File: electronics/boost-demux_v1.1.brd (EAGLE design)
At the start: 82.5 x 57.1 mm, 46 parts, among them M1 6-32_MOUNT, M2 6-32_MOUNT, M3 6-32_MOUNT, M4 6-32_MOUNT, Q1 ON_FDD4141, U1 TI_TPS55330, U2 4067D, U5 AVAGO_ACPL-217

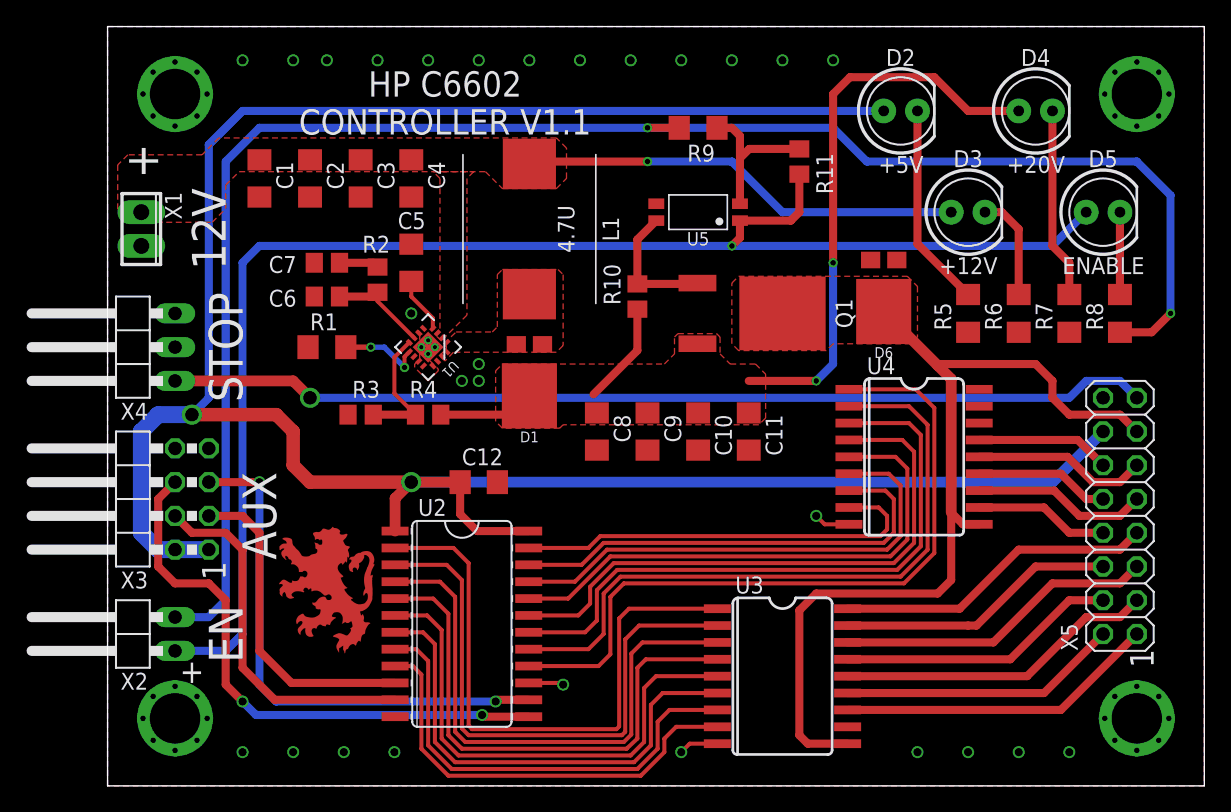
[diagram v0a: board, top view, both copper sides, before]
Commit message: Electronics v1.1 draft updates
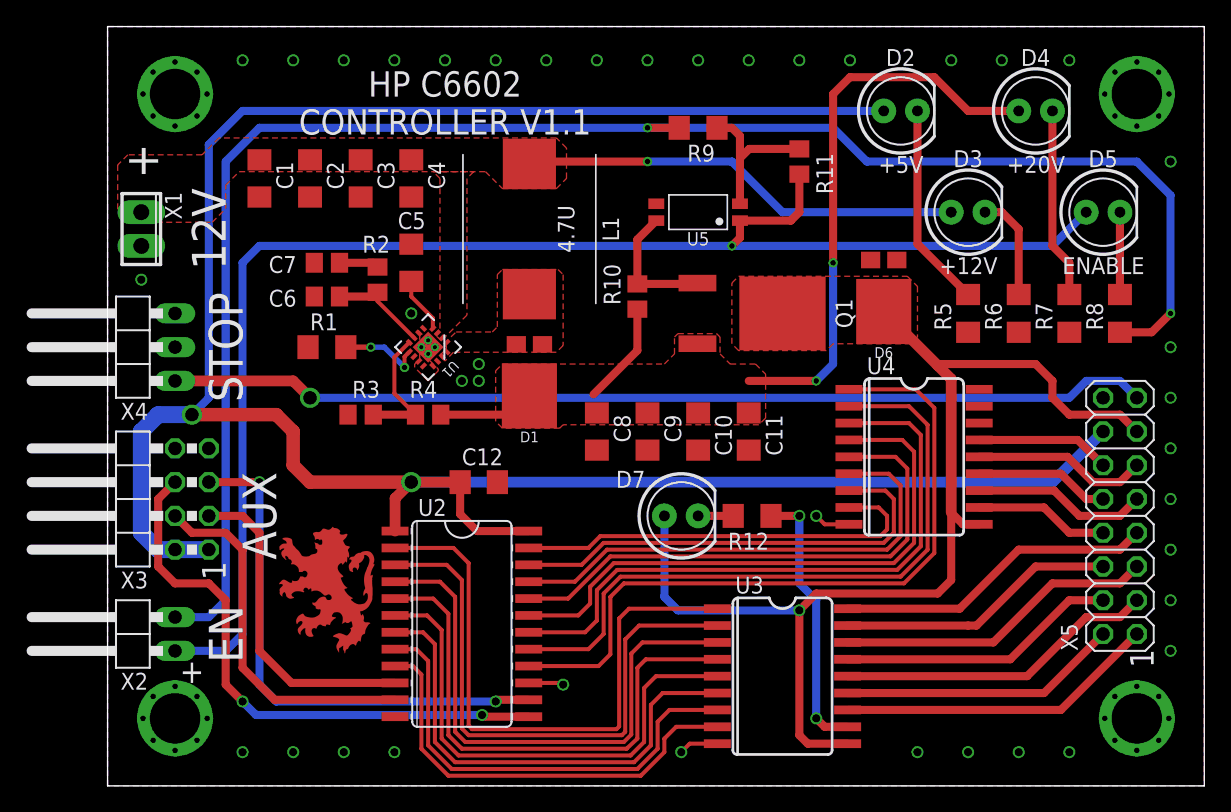
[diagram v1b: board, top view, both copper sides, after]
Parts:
- added D7: ACTIVITY, SparkFun-LED:LED_5MM
- added R12: 1k, resistor:R1206
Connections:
- new net N$12: R12.1, U3.11
- new net N$42: D7.K, R12.2
- net VCC: now also D7.A
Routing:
- net N$12: track 0.00 -> 20.5 mm, vias 0 -> 2
- net VCC: track 68.3 -> 85.0 mm, vias 0 -> 1
- net N$42: track 0.00 -> 2.64 mm
- net GND: vias 32 -> 44
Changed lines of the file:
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@@
 <layer number="17" name="Pads" color="2" fill="1" visible="yes" active="yes"/>
 <layer number="18" name="Vias" color="2" fill="1" visible="yes" active="yes"/>
-<layer number="19" name="Unrouted" color="6" fill="1" visible="no" active="yes"/>
+<layer number="19" name="Unrouted" color="6" fill="1" visible="yes" active="yes"/>
 <layer number="20" name="Dimension" color="15" fill="1" visible="yes" active="yes"/>
 <layer number="21" name="tPlace" color="7" fill="1" visible="yes" active="yes"/>
@@
 <element name="D1" library="components" package="TO-277-3" value="ON_FSV8100V" x="31.75" y="30.48" rot="R180"/>
 <element name="D2" library="SparkFun-LED" package="LED_5MM" value="+5V" x="59.69" y="50.8" smashed="yes">
-<attribute name="NAME" x="59.69" y="54.1909" size="1.27" layer="25" font="vector" ratio="10" align="bottom-center"/>
+<attribute name="NAME" x="59.69" y="54.1909" size="1.27" layer="21" font="vector" ratio="10" align="bottom-center"/>
 <attribute name="VALUE" x="59.7154" y="47.4091" size="1.27" layer="21" font="vector" ratio="10" align="top-center"/>
 </element>
 <element name="D3" library="SparkFun-LED" package="LED_5MM" value="+12V" x="64.77" y="43.18" smashed="yes">
-<attribute name="NAME" x="64.77" y="46.5709" size="1.27" layer="25" font="vector" ratio="10" align="bottom-center"/>
+<attribute name="NAME" x="64.77" y="46.5709" size="1.27" layer="21" font="vector" ratio="10" align="bottom-center"/>
 <attribute name="VALUE" x="64.7954" y="39.7891" size="1.27" layer="21" font="vector" ratio="10" align="top-center"/>
 </element>
 <element name="D4" library="SparkFun-LED" package="LED_5MM" value="+20V" x="69.85" y="50.8" smashed="yes">
-<attribute name="NAME" x="69.85" y="54.1909" size="1.27" layer="25" font="vector" ratio="10" align="bottom-center"/>
+<attribute name="NAME" x="69.85" y="54.1909" size="1.27" layer="21" font="vector" ratio="10" align="bottom-center"/>
 <attribute name="VALUE" x="69.8754" y="47.4091" size="1.27" layer="21" font="vector" ratio="10" align="top-center"/>
 </element>
 <element name="D5" library="SparkFun-LED" package="LED_5MM" value="ENABLE" x="74.93" y="43.18" smashed="yes">
-<attribute name="NAME" x="74.93" y="46.5709" size="1.27" layer="25" font="vector" ratio="10" align="bottom-center"/>
+<attribute name="NAME" x="74.93" y="46.5709" size="1.27" layer="21" font="vector" ratio="10" align="bottom-center"/>
 <attribute name="VALUE" x="74.9554" y="39.7891" size="1.27" layer="21" font="vector" ratio="10" align="top-center"/>
 </element>
@@
 <element name="M4" library="components" package="6-32_MOUNT" value="6-32_MOUNT" x="77.47" y="5.08"/>
 <element name="LOGO1" library="components" package="MADOG" value="MADOG" x="16.51" y="14.732"/>
+<element name="D7" library="SparkFun-LED" package="LED_5MM" value="ACTIVITY" x="43.18" y="20.32" smashed="yes">
+<attribute name="NAME" x="39.37" y="22.4409" size="1.27" layer="21" font="vector" ratio="10" align="bottom-center"/>
+<attribute name="VALUE" x="43.2054" y="16.9291" size="1.27" layer="27" font="vector" ratio="10" align="top-center"/>
+</element>
+<element name="R12" library="resistor" library_urn="urn:adsk.eagle:library:348" package="R1206" package3d_urn="urn:adsk.eagle:package:26062/1" value="1k" x="48.514" y="20.32" rot="R180"/>
 </elements>
 <signals>
@@
 <wire x1="31.93" y1="46.99" x2="31.75" y2="46.81" width="0.6096" layer="1"/>
 </signal>
-<signal name="GND" airwireshidden="yes">
+<signal name="GND">
 <contactref element="C1" pad="2"/>
 <contactref element="R1" pad="1"/>
@@
 <via x="10.16" y="54.61" extent="1-16" drill="0.6096"/>
 <via x="13.97" y="54.61" extent="1-16" drill="0.6096"/>
-<via x="20.32" y="54.61" extent="1-16" drill="0.6096"/>
-<via x="16.51" y="54.61" extent="1-16" drill="0.6096"/>
-<via x="24.13" y="54.61" extent="1-16" drill="0.6096"/>
-<via x="27.94" y="54.61" extent="1-16" drill="0.6096"/>
-<via x="31.75" y="54.61" extent="1-16" drill="0.6096"/>
-<via x="35.56" y="54.61" extent="1-16" drill="0.6096"/>
-<via x="39.37" y="54.61" extent="1-16" drill="0.6096"/>
-<via x="43.18" y="54.61" extent="1-16" drill="0.6096"/>
-<via x="46.99" y="54.61" extent="1-16" drill="0.6096"/>
-<via x="50.8" y="54.61" extent="1-16" drill="0.6096"/>
-<via x="54.61" y="54.61" extent="1-16" drill="0.6096"/>
+<via x="21.59" y="54.61" extent="1-16" drill="0.6096"/>
+<via x="17.78" y="54.61" extent="1-16" drill="0.6096"/>
+<via x="25.4" y="54.61" extent="1-16" drill="0.6096"/>
+<via x="29.21" y="54.61" extent="1-16" drill="0.6096"/>
+<via x="33.02" y="54.61" extent="1-16" drill="0.6096"/>
+<via x="36.83" y="54.61" extent="1-16" drill="0.6096"/>
+<via x="40.64" y="54.61" extent="1-16" drill="0.6096"/>
+<via x="44.45" y="54.61" extent="1-16" drill="0.6096"/>
+<via x="48.26" y="54.61" extent="1-16" drill="0.6096"/>
+<via x="52.07" y="54.61" extent="1-16" drill="0.6096"/>
+<via x="55.88" y="54.61" extent="1-16" drill="0.6096"/>
 <via x="10.16" y="2.54" extent="1-16" drill="0.6096"/>
 <via x="13.97" y="2.54" extent="1-16" drill="0.6096"/>
@@
 <via x="21.59" y="2.54" extent="1-16" drill="0.6096"/>
 <via x="26.67" y="30.48" extent="1-16" drill="0.6096"/>
+<via x="80.01" y="10.16" extent="1-16" drill="0.6096"/>
+<via x="80.01" y="13.97" extent="1-16" drill="0.6096"/>
+<via x="80.01" y="17.78" extent="1-16" drill="0.6096"/>
+<via x="80.01" y="21.59" extent="1-16" drill="0.6096"/>
+<via x="80.01" y="25.4" extent="1-16" drill="0.6096"/>
+<via x="80.01" y="29.21" extent="1-16" drill="0.6096"/>
+<via x="80.01" y="33.02" extent="1-16" drill="0.6096"/>
+<via x="80.01" y="46.99" extent="1-16" drill="0.6096"/>
+<via x="72.39" y="54.61" extent="1-16" drill="0.6096"/>
+<via x="63.5" y="54.61" extent="1-16" drill="0.6096"/>
+<via x="67.31" y="54.61" extent="1-16" drill="0.6096"/>
+<via x="2.54" y="38.1" extent="1-16" drill="0.6096"/>
 </signal>
 <signal name="N$1">
@@
 <wire x1="69.85" y1="31.75" x2="62.6289625" y2="31.75" width="0.6096" layer="1"/>
 <wire x1="62.6289625" y1="31.75" x2="62.50198125" y2="31.62301875" width="0.6096" layer="1"/>
+<contactref element="D7" pad="A"/>
+<wire x1="41.91" y1="20.32" x2="41.91" y2="14.224" width="0.6096" layer="16"/>
+<wire x1="41.91" y1="14.224" x2="42.926" y2="13.208" width="0.6096" layer="16"/>
+<wire x1="42.926" y1="13.208" x2="52.07" y2="13.208" width="0.6096" layer="16"/>
+<via x="52.07" y="13.208" extent="1-16" drill="0.6096"/>
 </signal>
 <signal name="N$6">
@@
 <wire x1="71.12" y1="40.64" x2="73.66" y2="43.18" width="0.6096" layer="16"/>
 </signal>
+<signal name="N$12">
+<contactref element="U3" pad="11"/>
+<contactref element="R12" pad="1"/>
+<wire x1="49.936" y1="20.32" x2="52.07" y2="20.32" width="0.6096" layer="1"/>
+<via x="52.07" y="20.32" extent="1-16" drill="0.6096"/>
+<wire x1="52.07" y1="20.32" x2="52.07" y2="15.24" width="0.6096" layer="16"/>
+<wire x1="52.07" y1="15.24" x2="53.34" y2="13.97" width="0.6096" layer="16"/>
+<wire x1="53.34" y1="13.97" x2="53.34" y2="5.08" width="0.6096" layer="16"/>
+<via x="53.34" y="5.08" extent="1-16" drill="0.6096"/>
+<wire x1="53.34" y1="5.08" x2="53.975" y2="4.445" width="0.6096" layer="1"/>
+<wire x1="53.975" y1="4.445" x2="55.7022" y2="4.445" width="0.6096" layer="1"/>
+</signal>
+<signal name="N$42">
+<contactref element="R12" pad="2"/>
+<contactref element="D7" pad="K"/>
+<wire x1="44.45" y1="20.32" x2="47.092" y2="20.32" width="0.6096" layer="1"/>
+</signal>
 </signals>

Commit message: PCBs v1.1 final
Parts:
- added TP1, TP2, TP3, TP4: TPB1,27, testpad:B1,27
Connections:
- net +12V: now also TP2.TP
- net +20V: now also TP3.TP
- net +5V: now also TP1.TP
- net GND: now also TP4.TP
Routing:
- net +12V: track 33.4 -> 45.1 mm
- net +5V: track 180.0 -> 186.1 mm, vias 2 -> 3
- net +20V: track 57.8 -> 63.4 mm
- net GND: vias 44 -> 45
